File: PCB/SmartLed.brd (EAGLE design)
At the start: 85.1 x 65.5 mm, 51 parts, among them IC2 DS1307, IC3 MEGA8-P, K1 G5LE, Q2 32.768khz, T1 BC337

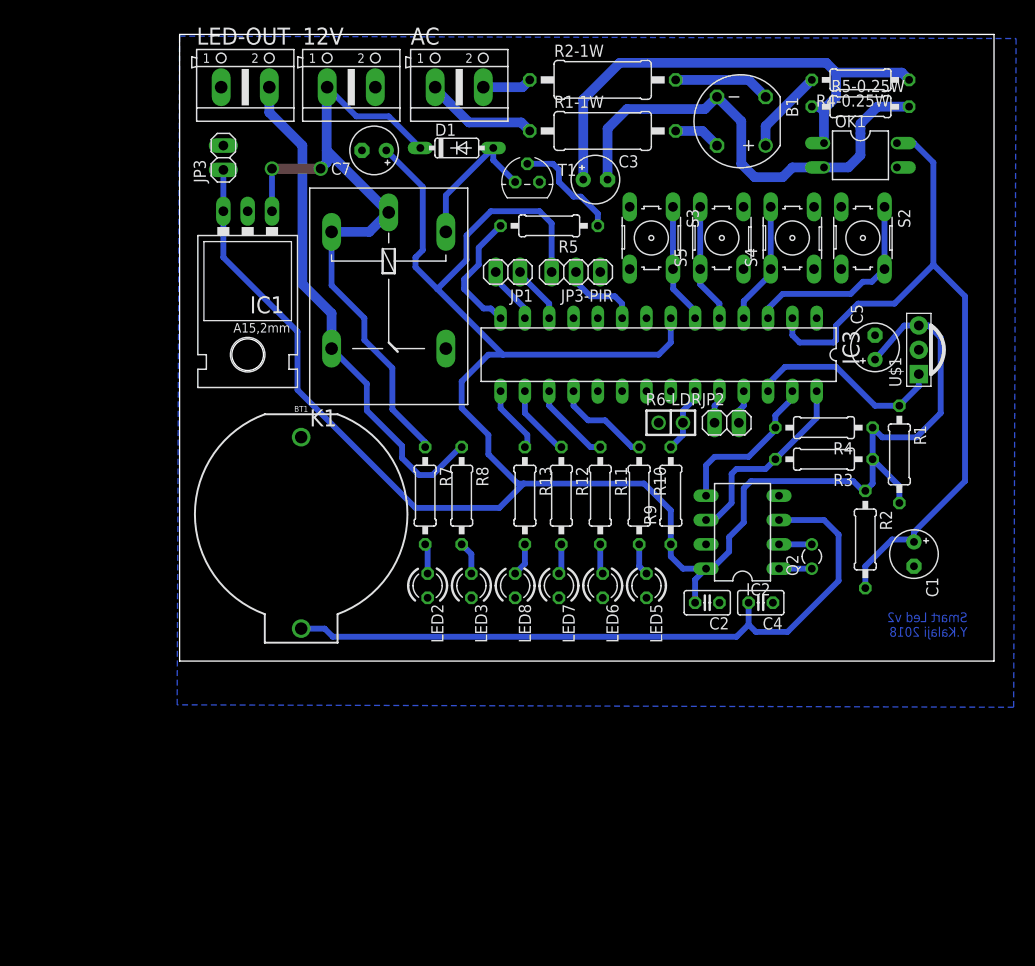
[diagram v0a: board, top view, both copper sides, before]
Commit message: Working on adding battery voltage meter & adding esp8266 connections header
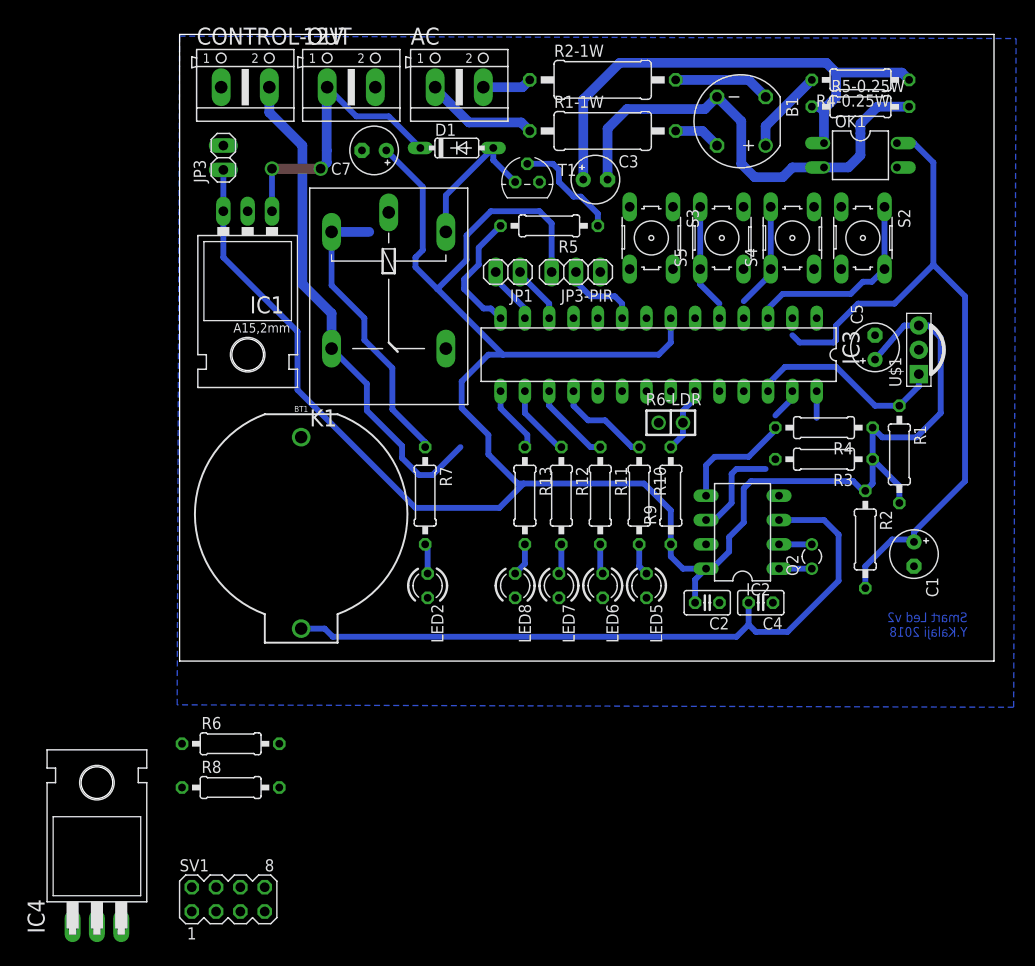
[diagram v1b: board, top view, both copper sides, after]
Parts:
- removed JP2: (no value), pinhead:1X02
- removed LED3: (no value), led:LED3MM
- added IC4: LM1117T(H)-3.3, lm1117_10:TO220H
- added R6: 100k, rcl:0207/10
- added SV1: (no value), con-lstb:MA04-2
- R8: value 1.2k -> 10k
- moved R8 38.9 mm to (1.78, 21.1), turned to 0 degrees
- renumbered LED-OUT to CONTROL-OUT
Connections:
- new net N$18: IC3.24, R6.2, R8.1
- net +12V: now also R6.1; no longer K1.P
- net GND: now also R8.2; no longer CONTROL-OUT.1, LED3.K
- net N$11: now also IC3.19; no longer IC3.2
- net N$16: now also CONTROL-OUT.1, K1.O; no longer LED3.A, R8.2
- net N$28: now also IC3.4; no longer IC3.3
- net N$30: now also IC3.3; no longer IC3.24, JP2.1
- net N$31: now also IC3.11; no longer IC3.6
- net N$32: now also IC3.5; no longer IC3.4
- net N$33: now also IC3.6; no longer IC3.5
- net N$34: now also IC3.2; no longer IC3.25, JP2.2
- net N$8: no longer R8.1
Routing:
- net N$31: track 12.6 -> 0.00 mm
- net +12V: track 73.7 -> 61.3 mm
- net N$12: track 20.6 -> 13.0 mm
- net N$34: track 4.27 -> 0.00 mm
- net N$30: track 3.51 -> 0.00 mm
- net N$16: track 3.47 -> 0.00 mm
- net N$32: track 13.8 -> 11.0 mm
- net N$11: track 77.6 -> 75.8 mm
- net N$33: track 12.5 -> 10.9 mm
- net N$13: track 16.7 -> 15.2 mm
- net N$28: track 21.5 -> 20.4 mm
